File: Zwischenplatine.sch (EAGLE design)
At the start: 3 parts

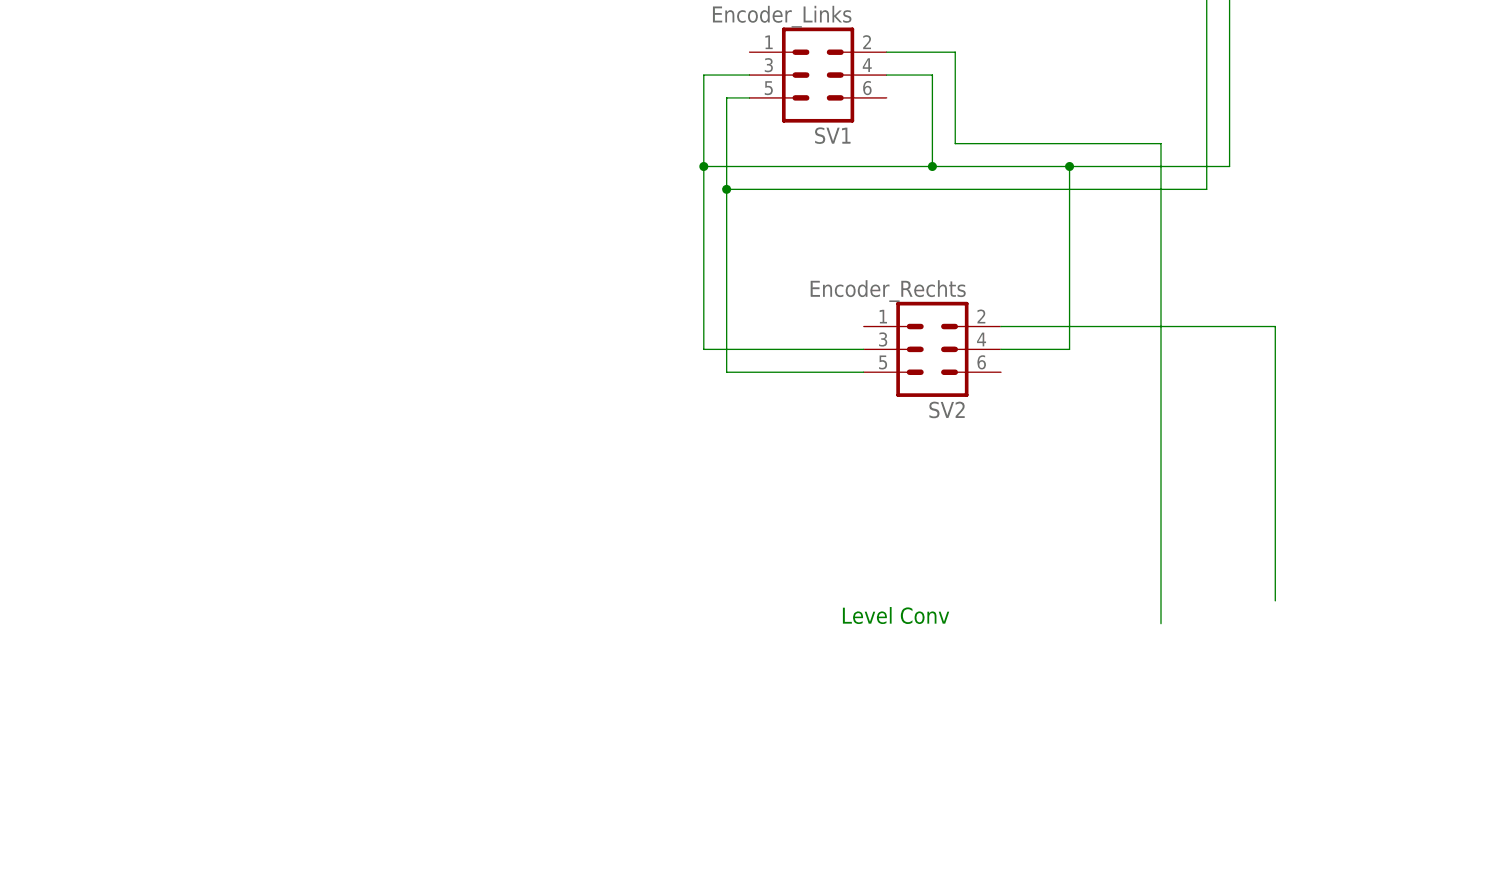
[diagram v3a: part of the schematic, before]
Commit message: 
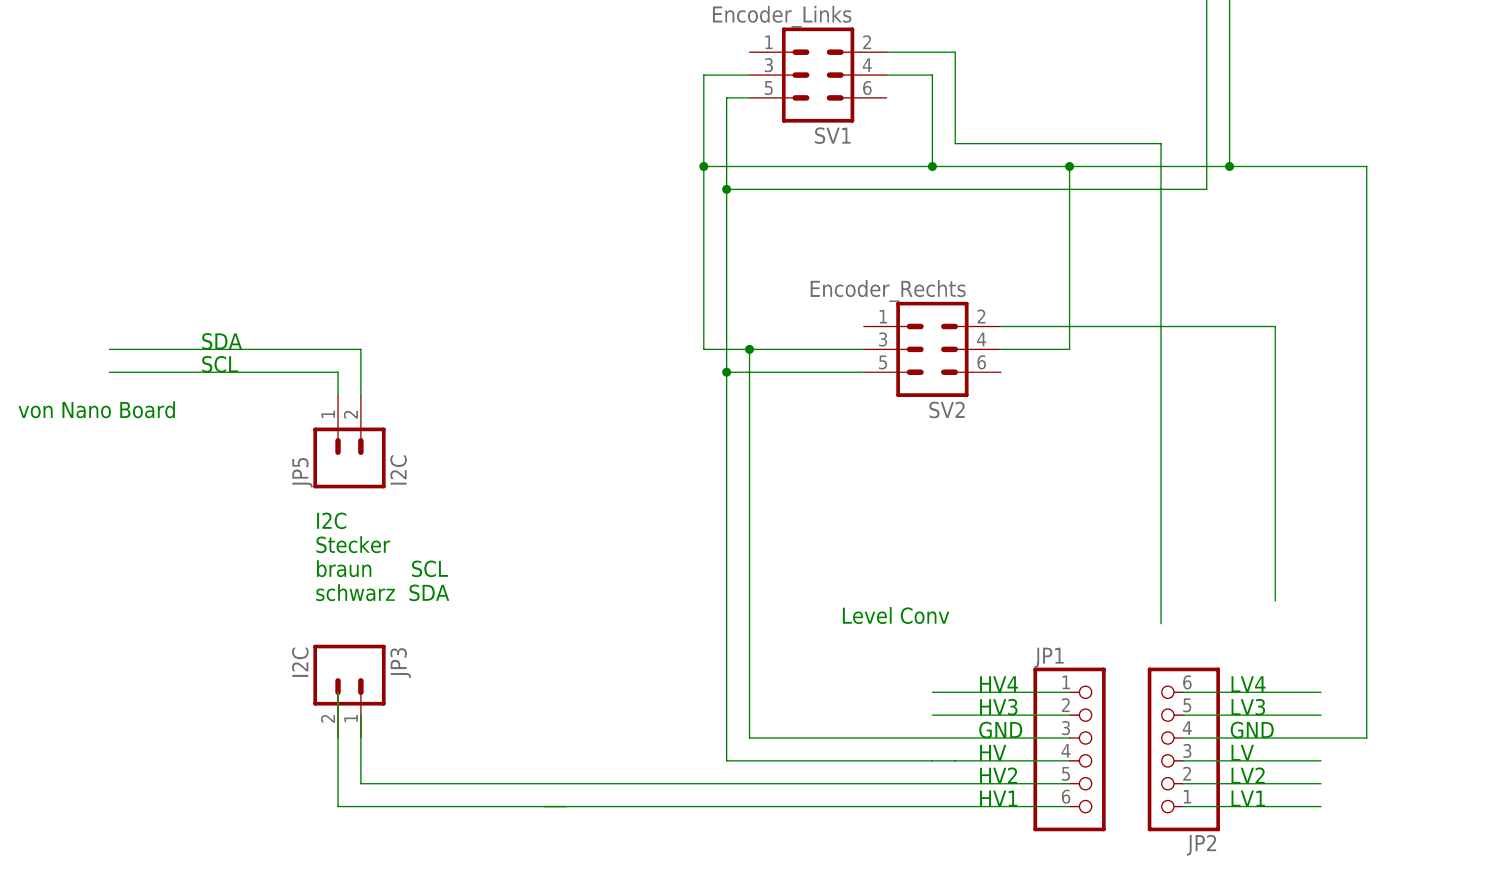
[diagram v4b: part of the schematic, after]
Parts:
- added JP1, JP2: (no value), adafruit:PINHD-1X6B
- added JP3, JP5: I2C, SparkFun-Connectors:M02-JST-2MM-SMT
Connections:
- new net N$10: JP2.5
- new net N$11: JP1.3, JP2.4, JP7.2, SV1.3, SV1.4, SV2.3, SV2.4
- new net N$12: JP2.3
- new net N$13: JP2.2
- new net N$14: JP2.1
- new net N$3: JP1.1
- new net N$4: JP1.2
- new net N$5: JP5.1
- new net N$7: JP1.5
- new net N$8: JP1.6
- new net N$9: JP2.6
- net N$1: now also JP1.4
- net N$2: now also JP5.2; no longer JP7.2, SV1.3, SV1.4, SV2.3, SV2.4
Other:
- note added: "HV"
- note added: "HV1"
- note added: "HV2"
- note added: "HV3"
- note added: "HV4"
- note added: "I2C Stecker braun SCL schwarz SDA"
- note added: "LV"
- note added: "LV1"
- note added: "LV2"
- note added: "LV3"
- note added: "LV4"
- note added: "SCL"
- note added: "SDA"
- note added: "von Nano Board"
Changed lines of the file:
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@@
 <layer number="56" name="wert" color="7" fill="1" visible="no" active="no"/>
 <layer number="57" name="tCAD" color="7" fill="1" visible="no" active="no"/>
+<layer number="88" name="SimResults" color="9" fill="1" visible="yes" active="yes"/>
+<layer number="89" name="SimProbes" color="9" fill="1" visible="yes" active="yes"/>
 <layer number="90" name="Modules" color="5" fill="1" visible="yes" active="yes"/>
 <layer number="91" name="Nets" color="2" fill="1" visible="yes" active="yes"/>
@@
 <part name="SV2" library="con-ml" deviceset="ML6" device="" value="Encoder_Rechts"/>
 <part name="JP7" library="SparkFun-Connectors" deviceset="M02" device="-JST-2MM-SMT" value="Spg"/>
+<part name="JP1" library="adafruit" deviceset="PINHD-1X6" device="B"/>
+<part name="JP2" library="adafruit" deviceset="PINHD-1X6" device="B"/>
+<part name="JP5" library="SparkFun-Connectors" deviceset="M02" device="-JST-2MM-SMT" value="I2C"/>
+<part name="JP3" library="SparkFun-Connectors" deviceset="M02" device="-JST-2MM-SMT" value="I2C"/>
 </parts>
 <sheets>
@@
 schwarz  5V</text>
 <text x="17.78" y="55.88" size="1.778" layer="91">Level Conv</text>
+<text x="33.02" y="35.56" size="1.778" layer="91">HV1</text>
+<text x="33.02" y="38.1" size="1.778" layer="91">HV2</text>
+<text x="33.02" y="40.64" size="1.778" layer="91">HV</text>
+<text x="33.02" y="43.18" size="1.778" layer="91">GND</text>
+<text x="33.02" y="45.72" size="1.778" layer="91">HV3</text>
+<text x="33.02" y="48.26" size="1.778" layer="91">HV4</text>
+<text x="60.96" y="35.56" size="1.778" layer="91">LV1</text>
+<text x="60.96" y="38.1" size="1.778" layer="91">LV2</text>
+<text x="60.96" y="40.64" size="1.778" layer="91">LV</text>
+<text x="60.96" y="43.18" size="1.778" layer="91">GND</text>
+<text x="60.96" y="45.72" size="1.778" layer="91">LV3</text>
+<text x="60.96" y="48.26" size="1.778" layer="91">LV4</text>
+<text x="-53.34" y="83.82" size="1.778" layer="91">SCL</text>
+<text x="-53.34" y="86.36" size="1.778" layer="91">SDA</text>
+<text x="-40.64" y="58.42" size="1.778" layer="91">I2C
+Stecker
+braun      SCL
+schwarz  SDA</text>
+<text x="-73.66" y="78.74" size="1.778" layer="91">von Nano Board</text>
 </plain>
 <instances>
@@
 </instance>
 <instance part="JP7" gate="G$1" x="58.42" y="147.32" rot="R270"/>
+<instance part="JP1" gate="A" x="45.72" y="40.64"/>
+<instance part="JP2" gate="A" x="53.34" y="43.18" rot="R180"/>
+<instance part="JP5" gate="G$1" x="-35.56" y="73.66" rot="R90"/>
+<instance part="JP3" gate="G$1" x="-38.1" y="50.8" rot="R270"/>
 </instances>
 <busses>
@@
 <wire x1="7.62" y1="114.3" x2="5.08" y2="114.3" width="0.1524" layer="91"/>
 <pinref part="SV2" gate="1" pin="5"/>
-</segment>
-</net>
-<net name="N$2" class="2">
-<segment>
+<wire x1="5.08" y1="83.82" x2="5.08" y2="40.64" width="0.1524" layer="91"/>
+<pinref part="JP1" gate="A" pin="4"/>
+<wire x1="43.18" y1="40.64" x2="30.48" y2="40.64" width="0.1524" layer="91"/>
+<wire x1="30.48" y1="40.64" x2="27.94" y2="40.64" width="0.1524" layer="91"/>
+<wire x1="5.08" y1="40.64" x2="27.94" y2="40.64" width="0.1524" layer="91"/>
+<junction x="5.08" y="83.82"/>
+</segment>
+</net>
+<net name="N$3" class="0">
+<segment>
+<pinref part="JP1" gate="A" pin="1"/>
+<wire x1="43.18" y1="48.26" x2="27.94" y2="48.26" width="0.1524" layer="91"/>
+</segment>
+</net>
+<net name="N$4" class="0">
+<segment>
+<pinref part="JP1" gate="A" pin="2"/>
+<wire x1="43.18" y1="45.72" x2="27.94" y2="45.72" width="0.1524" layer="91"/>
+</segment>
+</net>
+<net name="N$7" class="0">
+<segment>
+<pinref part="JP1" gate="A" pin="5"/>
+<wire x1="-35.56" y1="38.1" x2="-35.56" y2="45.72" width="0.1524" layer="91"/>
+<wire x1="43.18" y1="38.1" x2="-35.56" y2="38.1" width="0.1524" layer="91"/>
+</segment>
+</net>
+<net name="N$8" class="0">
+<segment>
+<pinref part="JP1" gate="A" pin="6"/>
+<wire x1="43.18" y1="35.56" x2="-15.24" y2="35.56" width="0.1524" layer="91"/>
+</segment>
+</net>
+<net name="N$9" class="0">
+<segment>
+<pinref part="JP2" gate="A" pin="6"/>
+<wire x1="55.88" y1="48.26" x2="71.12" y2="48.26" width="0.1524" layer="91"/>
+</segment>
+</net>
+<net name="N$10" class="0">
+<segment>
+<pinref part="JP2" gate="A" pin="5"/>
+<wire x1="55.88" y1="45.72" x2="71.12" y2="45.72" width="0.1524" layer="91"/>
+</segment>
+</net>
+<net name="N$11" class="0">
+<segment>
+<pinref part="JP2" gate="A" pin="4"/>
+<wire x1="55.88" y1="43.18" x2="76.2" y2="43.18" width="0.1524" layer="91"/>
+<wire x1="76.2" y1="43.18" x2="76.2" y2="106.68" width="0.1524" layer="91"/>
+<pinref part="JP1" gate="A" pin="3"/>
+<wire x1="43.18" y1="43.18" x2="7.62" y2="43.18" width="0.1524" layer="91"/>
 <wire x1="60.96" y1="139.7" x2="60.96" y2="106.68" width="0.1524" layer="91"/>
 <pinref part="SV1" gate="1" pin="3"/>
@@
 <wire x1="27.94" y1="116.84" x2="27.94" y2="106.68" width="0.1524" layer="91"/>
 <wire x1="2.54" y1="106.68" x2="2.54" y2="86.36" width="0.1524" layer="91"/>
-<wire x1="2.54" y1="86.36" x2="20.32" y2="86.36" width="0.1524" layer="91"/>
+<wire x1="2.54" y1="86.36" x2="7.62" y2="86.36" width="0.1524" layer="91"/>
+<wire x1="7.62" y1="86.36" x2="20.32" y2="86.36" width="0.1524" layer="91"/>
 <wire x1="43.18" y1="86.36" x2="43.18" y2="106.68" width="0.1524" layer="91"/>
 <junction x="2.54" y="106.68"/>
@@
 <pinref part="SV2" gate="1" pin="4"/>
 <wire x1="43.18" y1="86.36" x2="35.56" y2="86.36" width="0.1524" layer="91"/>
-</segment>
-</net>
+<wire x1="7.62" y1="43.18" x2="7.62" y2="86.36" width="0.1524" layer="91"/>
+<junction x="7.62" y="86.36"/>
+<wire x1="76.2" y1="106.68" x2="60.96" y2="106.68" width="0.1524" layer="91"/>
+<junction x="60.96" y="106.68"/>
+</segment>
+</net>
+<net name="N$12" class="0">
+<segment>
+<pinref part="JP2" gate="A" pin="3"/>
+<wire x1="55.88" y1="40.64" x2="71.12" y2="40.64" width="0.1524" layer="91"/>
+</segment>
+</net>
+<net name="N$13" class="0">
+<segment>
+<pinref part="JP2" gate="A" pin="2"/>
+<wire x1="55.88" y1="38.1" x2="71.12" y2="38.1" width="0.1524" layer="91"/>
+</segment>
+</net>
+<net name="N$14" class="0">
+<segment>
+<pinref part="JP2" gate="A" pin="1"/>
+<wire x1="55.88" y1="35.56" x2="71.12" y2="35.56" width="0.1524" layer="91"/>
+</segment>
+</net>
+<net name="N$2" class="0">
+<segment>
+<wire x1="-38.1" y1="83.82" x2="-38.1" y2="81.28" width="0.1524" layer="91"/>
+<pinref part="JP5" gate="G$1" pin="2"/>
+<wire x1="-63.5" y1="83.82" x2="-38.1" y2="83.82" width="0.1524" layer="91"/>
+</segment>
+</net>
+<net name="N$5" class="0">
+<segment>
+<wire x1="-63.5" y1="86.36" x2="-35.56" y2="86.36" width="0.1524" layer="91"/>
+<wire x1="-35.56" y1="86.36" x2="-35.56" y2="81.28" width="0.1524" layer="91"/>
+<pinref part="JP5" gate="G$1" pin="1"/>
+</segment>
+</net>
+<net name="N$15" class="0">
+<segment>
+<wire x1="-12.7" y1="35.56" x2="-38.1" y2="35.56" width="0.1524" layer="91"/>
+<wire x1="-38.1" y1="35.56" x2="-38.1" y2="48.26" width="0.1524" layer="91"/>
+</segment>
+</net>
